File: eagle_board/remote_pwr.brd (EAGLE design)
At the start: 24 x 30 mm, 9 parts

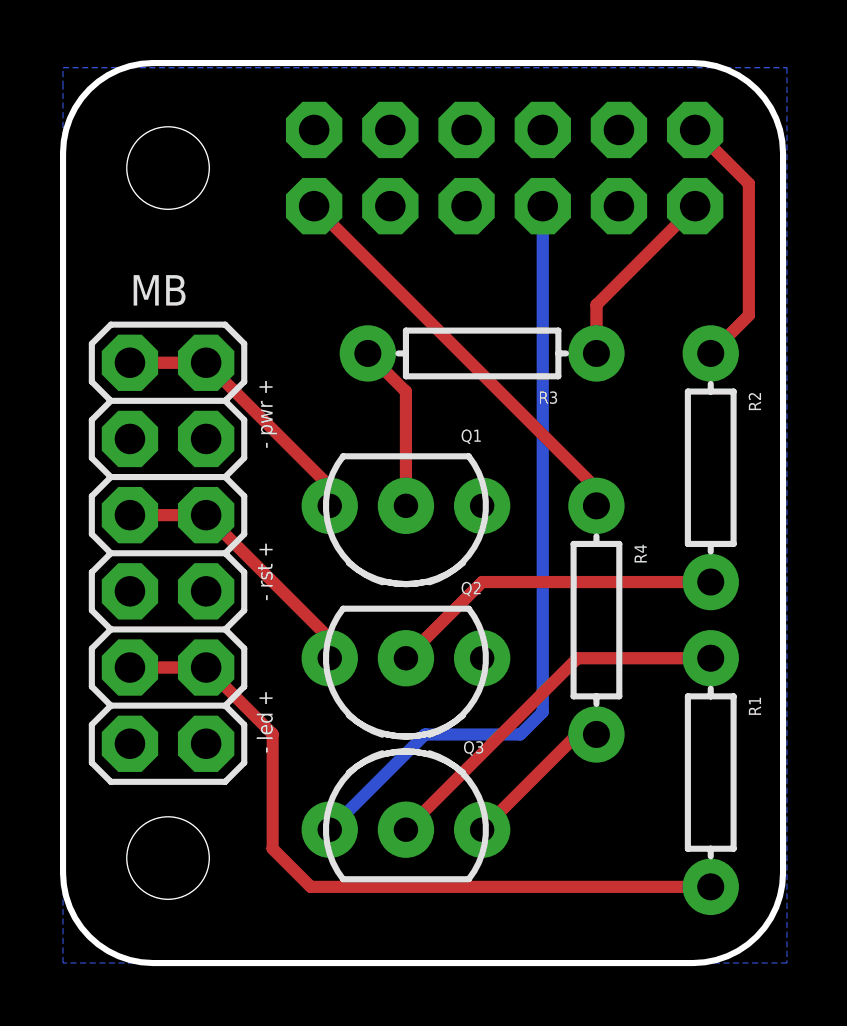
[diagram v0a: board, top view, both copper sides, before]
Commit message: Update EAGLE board
Change board to have all traces and ground plane on single side.
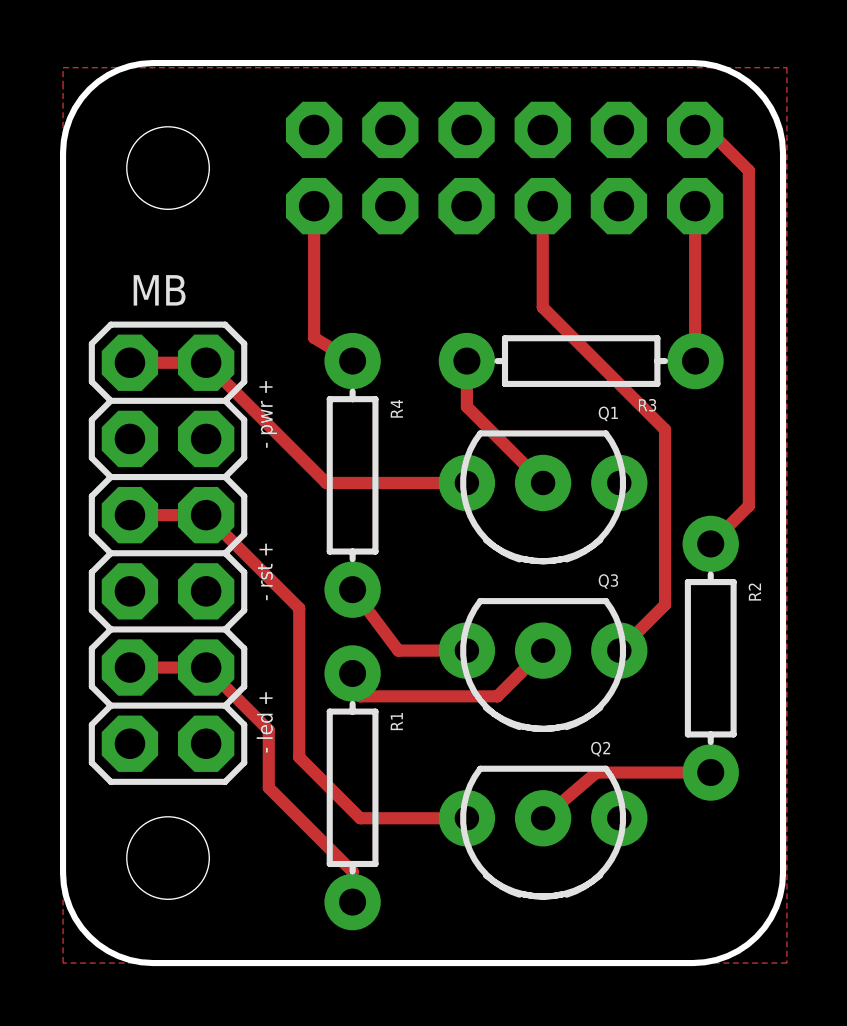
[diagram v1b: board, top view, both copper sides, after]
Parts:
- moved R1 11.9 mm to (9.65, 5.84)
- moved R4 9.45 mm to (9.65, 16.3)
- moved Q3 7.52 mm to (16.0, 10.4), turned to 180 degrees
- moved Q2 7.03 mm to (16.0, 4.83)
- moved R2 6.35 mm to (21.6, 10.2)
- moved Q1 4.64 mm to (16.0, 16.0)
- moved R3 3.31 mm to (17.3, 20.1)
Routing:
- net PWR_LED_POS: track 24.6 -> 12.4 mm
- net RST_BTN_POS: track 9.02 -> 18.3 mm
- net PWR_LED_IN: track 25.6 -> 17.1 mm
- net VCC: track 13.9 -> 5.89 mm
- net RST_BTN_OUT: track 8.72 -> 15.3 mm
- net N$3: track 11.2 -> 6.15 mm
- net N$4: track 12.5 -> 7.53 mm
- net PWR_BTN_POS: track 9.02 -> 12.9 mm
- net PWR_BTN_OUT: track 6.27 -> 5.17 mm
- added copper zone on layer 1, net GND
- removed copper zone on layer 16, net GND

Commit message: Update EAGLE board
Revert to old layout but still move traces to single side.
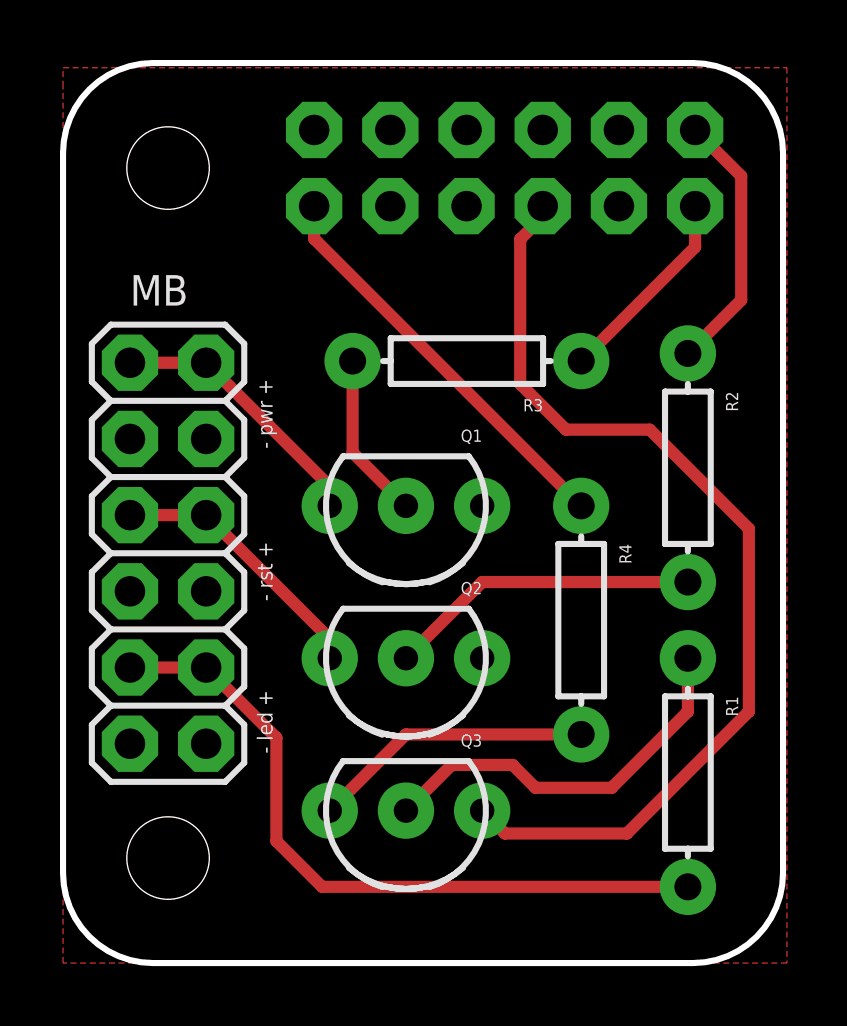
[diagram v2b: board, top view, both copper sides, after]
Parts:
- moved R1 11.2 mm to (20.8, 6.35)
- moved R4 9.02 mm to (17.3, 11.4)
- moved Q2 7.03 mm to (11.4, 10.2)
- moved Q3 7.03 mm to (11.4, 5.08)
- moved R2 6.40 mm to (20.8, 16.5)
- moved Q1 4.64 mm to (11.4, 15.2)
- moved R3 3.81 mm to (13.5, 20.1)
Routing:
- net PWR_LED_IN: track 17.1 -> 32.8 mm
- net PWR_LED_POS: track 12.4 -> 23.6 mm
- net RST_BTN_POS: track 18.3 -> 9.02 mm
- net VCC: track 5.89 -> 13.7 mm
- net RST_BTN_OUT: track 15.3 -> 8.82 mm
- net N$4: track 7.53 -> 13.2 mm
- net N$1: track 4.83 -> 9.43 mm
- net N$3: track 6.15 -> 10.5 mm
- net PWR_BTN_POS: track 12.9 -> 9.02 mm
- net PWR_BTN_OUT: track 5.17 -> 6.74 mm
